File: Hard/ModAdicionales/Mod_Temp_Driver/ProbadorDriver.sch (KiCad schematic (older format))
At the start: 4 parts

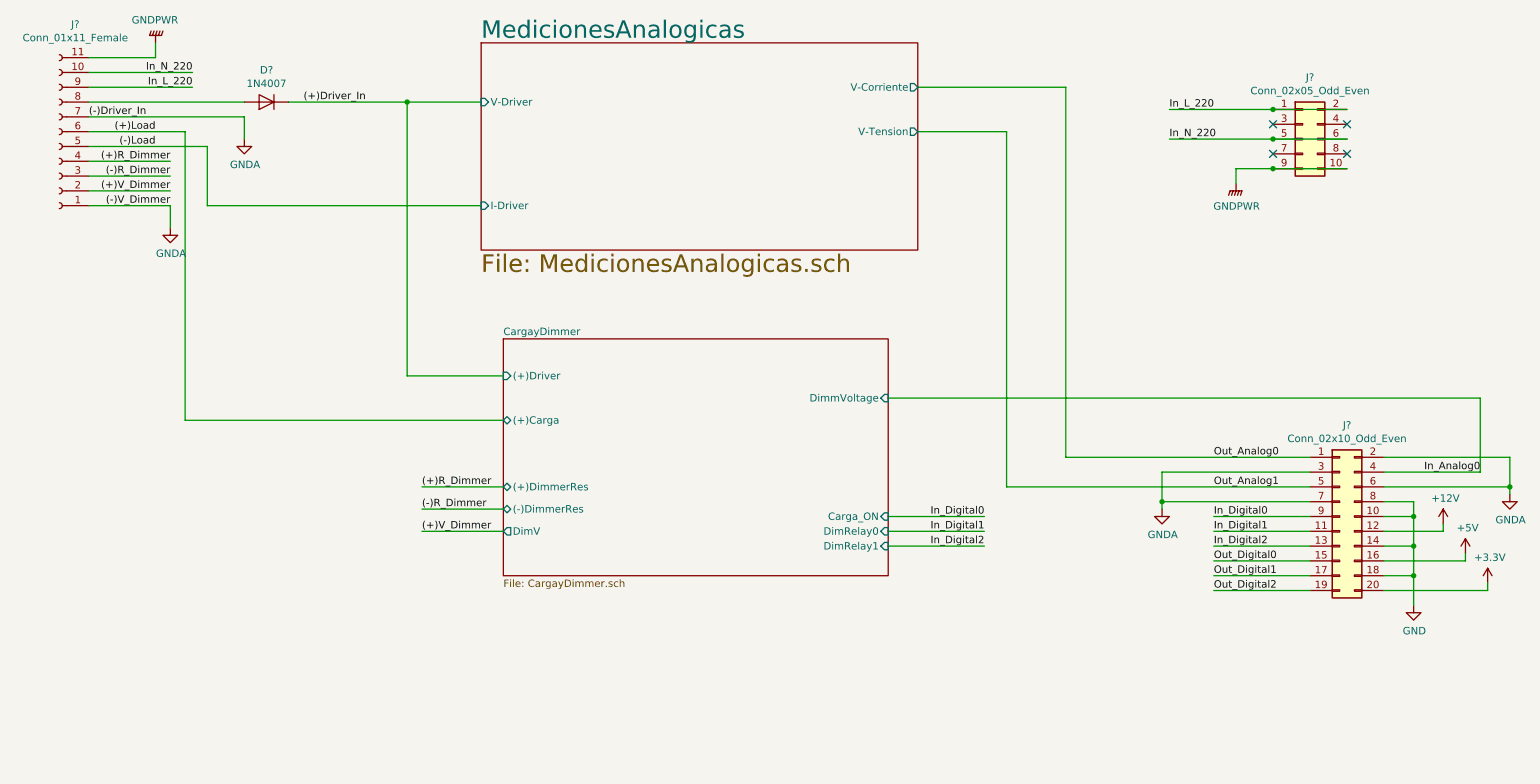
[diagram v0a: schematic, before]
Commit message: Primera correccion en modulos Adicionales y cambio de etapa de salida en modulo principal
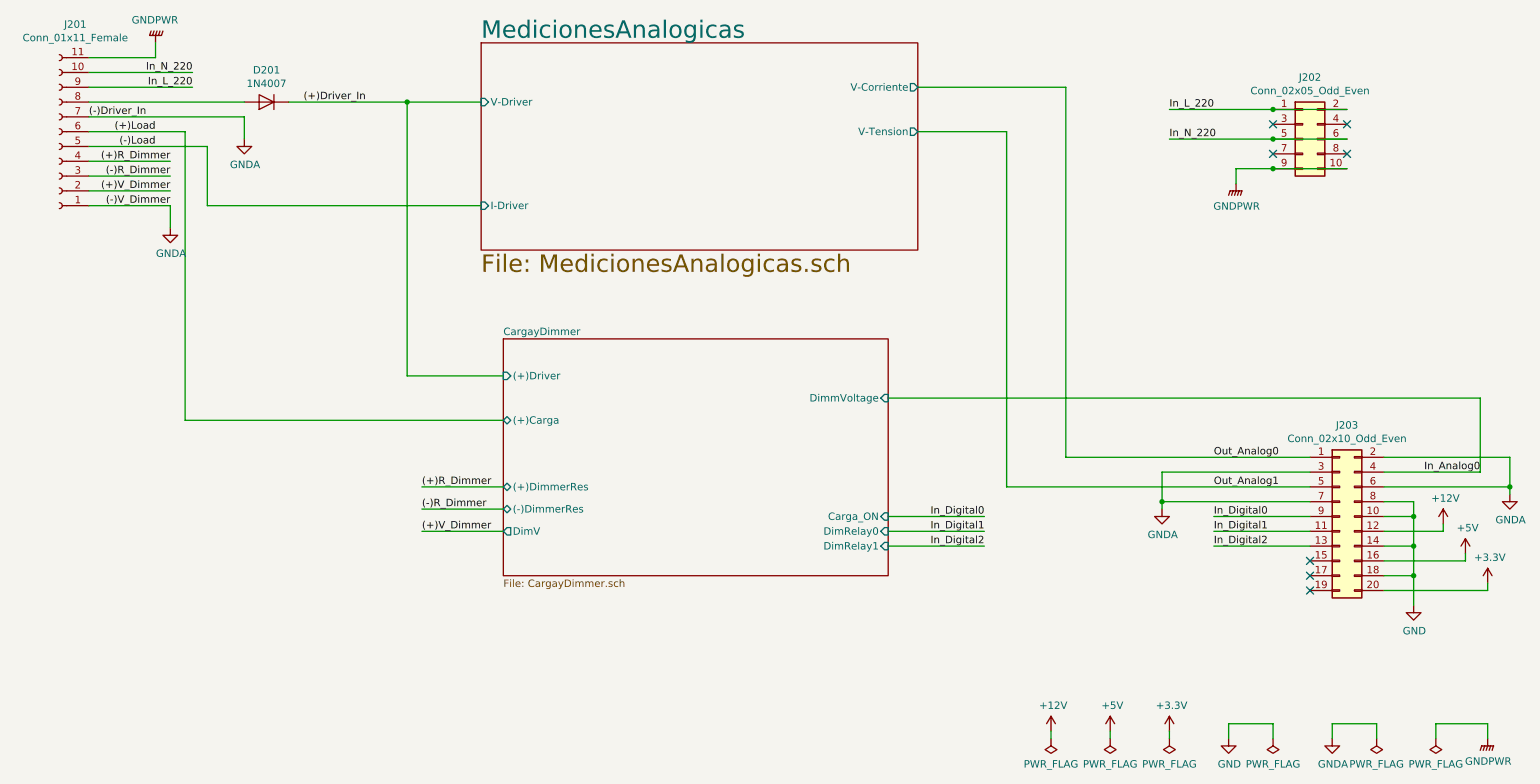
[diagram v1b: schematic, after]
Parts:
- gave numbers to parts that had none: 4
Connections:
- net Out_Digital0: no longer names the net of J203.15 (Pin_15)
- net Out_Digital1: no longer names the net of J203.17 (Pin_17)
- net Out_Digital2: no longer names the net of J203.19 (Pin_19)
- no-connect marks 4 -> 7
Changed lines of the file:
@@
 EESchema Schematic File Version 4
+LIBS:Mod_Temp_Driver-cache
 EELAYER 30 0
 EELAYER END
@@
 encoding utf-8
 Sheet 2 5
-Title ""
-Date ""
-Rev ""
-Comp ""
-Comment1 ""
+Title "Proyecto Final - Modulos Adicionales"
+Date "2020-06-02"
+Rev "1.0"
+Comp "CESE-FIUBA"
+Comment1 "Modulo Prueba de drivers"
 Comment2 ""
 Comment3 ""
@@
 $EndDescr
 $Comp
-L Connector_Generic:Conn_02x10_Odd_Even J?
+L Connector_Generic:Conn_02x10_Odd_Even J203
 U 1 1 5ED5A0E0
 P 9600 4650
-F 0 "J?" H 9650 5267 50  0000 C CNN
+F 0 "J203" H 9650 5267 50  0000 C CNN
 F 1 "Conn_02x10_Odd_Even" H 9650 5176 50  0000 C CNN
 F 2 "" H 9600 4650 50  0001 C CNN
@@
 Text Label 8750 4850 0    50   ~ 0
 In_Digital2
-Text Label 8750 4950 0    50   ~ 0
-Out_Digital0
-Text Label 8750 5050 0    50   ~ 0
-Out_Digital1
-Text Label 8750 5150 0    50   ~ 0
-Out_Digital2
 Text Label 10550 4350 2    50   ~ 0
 In_Analog0
 $Comp
-L power:+12V #PWR?
+L power:+12V #PWR0207
 U 1 1 5ED5A107
 P 10300 4700
-F 0 "#PWR?" H 10300 4550 50  0001 C CNN
+F 0 "#PWR0207" H 10300 4550 50  0001 C CNN
 F 1 "+12V" H 10315 4873 50  0000 C CNN
 F 2 "" H 10300 4700 50  0001 C CNN
@@
 $EndComp
 $Comp
-L power:+5V #PWR?
+L power:+5V #PWR0208
 U 1 1 5ED5A10D
 P 10450 4900
-F 0 "#PWR?" H 10450 4750 50  0001 C CNN
+F 0 "#PWR0208" H 10450 4750 50  0001 C CNN
 F 1 "+5V" H 10465 5073 50  0000 C CNN
 F 2 "" H 10450 4900 50  0001 C CNN
@@
 $EndComp
 $Comp
-L power:+3.3V #PWR?
+L power:+3.3V #PWR0209
 U 1 1 5ED5A113
 P 10600 5100
-F 0 "#PWR?" H 10600 4950 50  0001 C CNN
+F 0 "#PWR0209" H 10600 4950 50  0001 C CNN
 F 1 "+3.3V" H 10615 5273 50  0000 C CNN
 F 2 "" H 10600 5100 50  0001 C CNN
@@
 $EndComp
 $Comp
-L power:GND #PWR?
+L power:GND #PWR0206
 U 1 1 5ED5A119
 P 10100 5250
-F 0 "#PWR?" H 10100 5000 50  0001 C CNN
+F 0 "#PWR0206" H 10100 5000 50  0001 C CNN
 F 1 "GND" H 10105 5077 50  0000 C CNN
 F 2 "" H 10100 5250 50  0001 C CNN
@@
 $EndComp
 $Comp
-L power:GNDA #PWR?
+L power:GNDA #PWR0204
 U 1 1 5ED5A11F
 P 8400 4600
-F 0 "#PWR?" H 8400 4350 50  0001 C CNN
+F 0 "#PWR0204" H 8400 4350 50  0001 C CNN
 F 1 "GNDA" H 8405 4427 50  0000 C CNN
 F 2 "" H 8400 4600 50  0001 C CNN
@@
 	8400 4550 8400 4600
 $Comp
-L power:GNDA #PWR?
+L power:GNDA #PWR0210
 U 1 1 5ED5A12A
 P 10750 4500
-F 0 "#PWR?" H 10750 4250 50  0001 C CNN
+F 0 "#PWR0210" H 10750 4250 50  0001 C CNN
 F 1 "GNDA" H 10755 4327 50  0000 C CNN
 F 2 "" H 10750 4500 50  0001 C CNN
@@
 	10100 5050 10100 5250
 Wire Wire Line
-	9900 5150 10600 5150
-Wire Wire Line
 	10600 5150 10600 5100
 Wire Wire Line
-	9900 4950 10450 4950
-Wire Wire Line
 	10450 4950 10450 4900
 Wire Wire Line
-	9900 4750 10300 4750
-Wire Wire Line
 	10300 4750 10300 4700
 Wire Wire Line
@@
 Wire Wire Line
 	8750 4850 9400 4850
-Wire Wire Line
-	9400 4950 8750 4950
-Wire Wire Line
-	8750 5050 9400 5050
-Wire Wire Line
-	9400 5150 8750 5150
 Text Label 2600 1850 0    50   ~ 0
 (+)Driver_In
 $Comp
-L Connector:Conn_01x11_Female J?
+L Connector:Conn_01x11_Female J201
 U 1 1 5EDA75F8
 P 950 2050
-F 0 "J?" H 842 1325 50  0000 C CNN
+F 0 "J201" H 842 1325 50  0000 C CNN
 F 1 "Conn_01x11_Female" H 842 1416 50  0000 C CNN
 F 2 "" H 950 2050 50  0001 C CNN
@@
 	1600 1450 1600 1550
 $Comp
-L power:GNDPWR #PWR?
+L power:GNDPWR #PWR0201
 U 1 1 5EDAAA7D
 P 1600 1450
-F 0 "#PWR?" H 1600 1250 50  0001 C CNN
+F 0 "#PWR0201" H 1600 1250 50  0001 C CNN
 F 1 "GNDPWR" H 1604 1296 50  0000 C CNN
 F 2 "" H 1600 1400 50  0001 C CNN
@@
 	2200 1950 2200 2100
 $Comp
-L power:GNDA #PWR?
+L power:GNDA #PWR0203
 U 1 1 5EDB7AE8
 P 2200 2100
-F 0 "#PWR?" H 2200 1850 50  0001 C CNN
+F 0 "#PWR0203" H 2200 1850 50  0001 C CNN
 F 1 "GNDA" H 2205 1927 50  0000 C CNN
 F 2 "" H 2200 2100 50  0001 C CNN
@@
 (-)V_Dimmer
 $Comp
-L Diode:1N4007 D?
+L Diode:1N4007 D201
 U 1 1 5EFCD671
 P 2350 1850
-F 0 "D?" H 2350 1634 50  0000 C CNN
+F 0 "D201" H 2350 1634 50  0000 C CNN
 F 1 "1N4007" H 2350 1725 50  0000 C CNN
 F 2 "Diode_THT:D_DO-41_SOD81_P10.16mm_Horizontal" H 2350 1675 50  0001 C CNN
@@
 $EndSheet
 $Comp
-L Connector_Generic:Conn_02x05_Odd_Even J?
+L Connector_Generic:Conn_02x05_Odd_Even J202
 U 1 1 5F1BC542
 P 9350 2100
-AR Path="/5ED5374F/5F1BC542" Ref="J?"  Part="1"
+AR Path="/5ED5374F/5F1BC542" Ref="J202"  Part="1"
 AR Path="/5ED5374F/5F0ECABF/5F1BC542" Ref="J?"  Part="1"
-F 0 "J?" H 9400 2517 50  0000 C CNN
+F 0 "J202" H 9400 2517 50  0000 C CNN
 F 1 "Conn_02x05_Odd_Even" H 9400 2426 50  0000 C CNN
 F 2 "" H 9350 2100 50  0001 C CNN
@@
 In_L_220
 $Comp
-L power:GNDPWR #PWR?
+L power:GNDPWR #PWR0205
 U 1 1 5F1BC54A
 P 8900 2400
-AR Path="/5ED5374F/5F1BC54A" Ref="#PWR?"  Part="1"
+AR Path="/5ED5374F/5F1BC54A" Ref="#PWR0205"  Part="1"
 AR Path="/5ED5374F/5F0ECABF/5F1BC54A" Ref="#PWR?"  Part="1"
-F 0 "#PWR?" H 8900 2200 50  0001 C CNN
+F 0 "#PWR0205" H 8900 2200 50  0001 C CNN
 F 1 "GNDPWR" H 8904 2246 50  0000 C CNN
 F 2 "" H 8900 2350 50  0001 C CNN
@@
 	1700 2550 1700 2700
 $Comp
-L power:GNDA #PWR?
+L power:GNDA #PWR0202
 U 1 1 5F3DBE4C
 P 1700 2700
-F 0 "#PWR?" H 1700 2450 50  0001 C CNN
+F 0 "#PWR0202" H 1700 2450 50  0001 C CNN
 F 1 "GNDA" H 1705 2527 50  0000 C CNN
 F 2 "" H 1700 2700 50  0001 C CNN
@@
 	1    0    0    -1
 $EndComp
+NoConn ~ 9400 4950
+NoConn ~ 9400 5050
+NoConn ~ 9400 5150
+$Comp
+L power:+12V #PWR0101
+U 1 1 5EE6D5BC
+P 7650 6100
+F 0 "#PWR0101" H 7650 5950 50  0001 C CNN
+F 1 "+12V" H 7665 6273 50  0000 C CNN
+F 2 "" H 7650 6100 50  0001 C CNN
+F 3 "" H 7650 6100 50  0001 C CNN
+	1    7650 6100
+	1    0    0    -1
+$EndComp
+$Comp
+L power:+5V #PWR0102
+U 1 1 5EE6D5C2
+P 8050 6100
+F 0 "#PWR0102" H 8050 5950 50  0001 C CNN
+F 1 "+5V" H 8065 6273 50  0000 C CNN
+F 2 "" H 8050 6100 50  0001 C CNN
+F 3 "" H 8050 6100 50  0001 C CNN
+	1    8050 6100
+	1    0    0    -1
+$EndComp
+$Comp
+L power:+3.3V #PWR0103
+U 1 1 5EE6D5C8
+P 8450 6100
+F 0 "#PWR0103" H 8450 5950 50  0001 C CNN
+F 1 "+3.3V" H 8465 6273 50  0000 C CNN
+F 2 "" H 8450 6100 50  0001 C CNN
+F 3 "" H 8450 6100 50  0001 C CNN
+	1    8450 6100
+	1    0    0    -1
+$EndComp
+Wire Wire Line
+	8450 6150 8450 6100
+Wire Wire Line
+	8050 6150 8050 6100
+Wire Wire Line
+	7650 6150 7650 6100
+$Comp
+L power:PWR_FLAG #FLG0101
+U 1 1 5EE6D5D4
+P 8050 6150
+F 0 "#FLG0101" H 8050 6225 50  0001 C CNN
+F 1 "PWR_FLAG" H 8050 6323 50  0000 C CNN
+F 2 "" H 8050 6150 50  0001 C CNN
+F 3 "~" H 8050 6150 50  0001 C CNN
+	1    8050 6150
+	-1   0    0    1
+$EndComp
+$Comp
+L power:PWR_FLAG #FLG0102
+U 1 1 5EE6D5DC
+P 7650 6150
+F 0 "#FLG0102" H 7650 6225 50  0001 C CNN
+F 1 "PWR_FLAG" H 7650 6323 50  0000 C CNN
+F 2 "" H 7650 6150 50  0001 C CNN
+F 3 "~" H 7650 6150 50  0001 C CNN
+	1    7650 6150
+	-1   0    0    1
+$EndComp
+$Comp
+L power:PWR_FLAG #FLG0103
+U 1 1 5EE823D4
+P 8450 6150
+F 0 "#FLG0103" H 8450 6225 50  0001 C CNN
+F 1 "PWR_FLAG" H 8450 6323 50  0000 C CNN
+F 2 "" H 8450 6150 50  0001 C CNN
+F 3 "~" H 8450 6150 50  0001 C CNN
+	1    8450 6150
+	-1   0    0    1
+$EndComp
+$Comp
+L power:GND #PWR0104
+U 1 1 5EE8980A
+P 8850 6150
+F 0 "#PWR0104" H 8850 5900 50  0001 C CNN
+F 1 "GND" H 8855 5977 50  0000 C CNN
+F 2 "" H 8850 6150 50  0001 C CNN
+F 3 "" H 8850 6150 50  0001 C CNN
+	1    8850 6150
+	1    0    0    -1
+$EndComp
+$Comp
+L power:PWR_FLAG #FLG0106
+U 1 1 5EE8BBA8
+P 9150 6150
+F 0 "#FLG0106" H 9150 6225 50  0001 C CNN
+F 1 "PWR_FLAG" H 9150 6323 50  0000 C CNN
+F 2 "" H 9150 6150 50  0001 C CNN
+F 3 "~" H 9150 6150 50  0001 C CNN
+	1    9150 6150
+	-1   0    0    1
+$EndComp
+Wire Wire Line
+	9150 6150 9150 6050
+Wire Wire Line
+	9150 6050 8850 6050
+Wire Wire Line
+	8850 6050 8850 6150
+Wire Wire Line
+	9900 5150 10600 5150
+Wire Wire Line
+	9900 4950 10450 4950
+Wire Wire Line
+	9900 4750 10300 4750
+$Comp
+L power:PWR_FLAG #FLG0107
+U 1 1 5EE96E0D
+P 9850 6150
+F 0 "#FLG0107" H 9850 6225 50  0001 C CNN
+F 1 "PWR_FLAG" H 9850 6323 50  0000 C CNN
+F 2 "" H 9850 6150 50  0001 C CNN
+F 3 "~" H 9850 6150 50  0001 C CNN
+	1    9850 6150
+	-1   0    0    1
+$EndComp
+Wire Wire Line
+	9850 6150 9850 6050
+Wire Wire Line
+	9850 6050 9550 6050
+Wire Wire Line
+	9550 6050 9550 6150
+$Comp
+L power:GNDA #PWR0105
+U 1 1 5EE9BBA8
+P 9550 6150
+F 0 "#PWR0105" H 9550 5900 50  0001 C CNN
+F 1 "GNDA" H 9555 5977 50  0000 C CNN
+F 2 "" H 9550 6150 50  0001 C CNN
+F 3 "" H 9550 6150 50  0001 C CNN
+	1    9550 6150
+	1    0    0    -1
+$EndComp
+$Comp
+L power:GNDPWR #PWR0107
+U 1 1 5EEDA7EC
+P 10600 6150
+F 0 "#PWR0107" H 10600 5950 50  0001 C CNN
+F 1 "GNDPWR" H 10604 5996 50  0000 C CNN
+F 2 "" H 10600 6100 50  0001 C CNN
+F 3 "" H 10600 6100 50  0001 C CNN
+	1    10600 6150
+	1    0    0    -1
+$EndComp
+$Comp
+L power:PWR_FLAG #FLG0105
+U 1 1 5EEDA7F2
+P 10250 6150
+F 0 "#FLG0105" H 10250 6225 50  0001 C CNN
+F 1 "PWR_FLAG" H 10250 6323 50  0000 C CNN
+F 2 "" H 10250 6150 50  0001 C CNN
+F 3 "~" H 10250 6150 50  0001 C CNN
+	1    10250 6150
+	-1   0    0    1
+$EndComp
+Wire Wire Line
+	10250 6050 10600 6050
+Wire Wire Line
+	10600 6050 10600 6150
+Wire Wire Line
+	10250 6050 10250 6150
 $EndSCHEMATC

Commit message: Asignacion de footprints Modulos adicionales
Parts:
- J201: footprint (none) -> TerminalBlock_Altech:Altech_AK300_1x11_P5.00mm_45-Degree
- J202: footprint (none) -> Connector_PinHeader_2.54mm:PinHeader_2x05_P2.54mm_Horizontal
- J203: footprint (none) -> Connector_PinHeader_2.54mm:PinHeader_2x10_P2.54mm_Horizontal
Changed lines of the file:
@@
 F 0 "J203" H 9650 5267 50  0000 C CNN
 F 1 "Conn_02x10_Odd_Even" H 9650 5176 50  0000 C CNN
-F 2 "" H 9600 4650 50  0001 C CNN
+F 2 "Connector_PinHeader_2.54mm:PinHeader_2x10_P2.54mm_Horizontal" H 9600 4650 50  0001 C CNN
 F 3 "~" H 9600 4650 50  0001 C CNN
 	1    9600 4650
@@
 F 0 "J201" H 842 1325 50  0000 C CNN
 F 1 "Conn_01x11_Female" H 842 1416 50  0000 C CNN
-F 2 "" H 950 2050 50  0001 C CNN
+F 2 "TerminalBlock_Altech:Altech_AK300_1x11_P5.00mm_45-Degree" H 950 2050 50  0001 C CNN
 F 3 "~" H 950 2050 50  0001 C CNN
 	1    950  2050
@@
 F 0 "J202" H 9400 2517 50  0000 C CNN
 F 1 "Conn_02x05_Odd_Even" H 9400 2426 50  0000 C CNN
-F 2 "" H 9350 2100 50  0001 C CNN
+F 2 "Connector_PinHeader_2.54mm:PinHeader_2x05_P2.54mm_Horizontal" H 9350 2100 50  0001 C CNN
 F 3 "~" H 9350 2100 50  0001 C CNN
 	1    9350 2100

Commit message: Inicio placement de componentes en Modulos Adicionales
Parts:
- added H201, H202, H203, H204: MountingHole, MountingHole:MountingHole_3.2mm_M3, symbol Mechanical:MountingHole
- J201: footprint TerminalBlock_Altech:Altech_AK300_1x11_P5.00mm_45-Degree -> Conectores:TerminalBlock_bornier-11_P5.00mm
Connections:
- net (+)R_Dimmer: now also J201.8 (Pin_8); no longer J201.4 (Pin_4)
- net (+)V_Dimmer: now also J201.10 (Pin_10); no longer J201.2 (Pin_2)
- net (-)Load: now also J201.7 (Pin_7); no longer J201.5 (Pin_5)
- net (-)R_Dimmer: now also J201.9 (Pin_9); no longer J201.3 (Pin_3)
- net GNDA: now also J201.11 (Pin_11), J201.5 (Pin_5); no longer J201.1 (Pin_1), J201.7 (Pin_7)
- net GNDPWR: now also J201.1 (Pin_1); no longer J201.11 (Pin_11)
- net In_L_220: now also J201.3 (Pin_3); no longer J201.9 (Pin_9)
- net In_N_220: now also J201.2 (Pin_2); no longer J201.10 (Pin_10)
- net at D201.2 (A): now also J201.4 (Pin_4); no longer J201.8 (Pin_8)
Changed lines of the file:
@@
 EESchema Schematic File Version 4
-LIBS:Mod_Temp_Driver-cache
 EELAYER 30 0
 EELAYER END
@@
 Comment4 ""
 $EndDescr
-$Comp
-L Connector_Generic:Conn_02x10_Odd_Even J203
-U 1 1 5ED5A0E0
-P 9600 4650
-F 0 "J203" H 9650 5267 50  0000 C CNN
-F 1 "Conn_02x10_Odd_Even" H 9650 5176 50  0000 C CNN
-F 2 "Connector_PinHeader_2.54mm:PinHeader_2x10_P2.54mm_Horizontal" H 9600 4650 50  0001 C CNN
-F 3 "~" H 9600 4650 50  0001 C CNN
-	1    9600 4650
-	1    0    0    -1
-$EndComp
 Text Label 8750 4250 0    50   ~ 0
 Out_Analog0
@@
 Text Label 2600 1850 0    50   ~ 0
 (+)Driver_In
-$Comp
-L Connector:Conn_01x11_Female J201
-U 1 1 5EDA75F8
-P 950 2050
-F 0 "J201" H 842 1325 50  0000 C CNN
-F 1 "Conn_01x11_Female" H 842 1416 50  0000 C CNN
-F 2 "TerminalBlock_Altech:Altech_AK300_1x11_P5.00mm_45-Degree" H 950 2050 50  0001 C CNN
-F 3 "~" H 950 2050 50  0001 C CNN
-	1    950  2050
-	-1   0    0    1
-$EndComp
 Text Label 1850 1650 2    50   ~ 0
 In_N_220
@@
 	1    0    0    -1
 $EndComp
-Text Label 1600 2050 2    50   ~ 0
-(+)Load
-Text Label 1600 2150 2    50   ~ 0
-(-)Load
 Text Label 1700 2250 2    50   ~ 0
 (+)R_Dimmer
@@
 Text Label 1700 2550 2    50   ~ 0
 (-)V_Dimmer
-$Comp
-L Diode:1N4007 D201
-U 1 1 5EFCD671
-P 2350 1850
-F 0 "D201" H 2350 1634 50  0000 C CNN
-F 1 "1N4007" H 2350 1725 50  0000 C CNN
-F 2 "Diode_THT:D_DO-41_SOD81_P10.16mm_Horizontal" H 2350 1675 50  0001 C CNN
-F 3 "http://www.vishay.com/docs/88503/1n4001.pdf" H 2350 1850 50  0001 C CNN
-	1    2350 1850
-	-1   0    0    1
-$EndComp
 Wire Wire Line
 	1150 1850 2200 1850
@@
 F5 "V-Driver" I L 3800 1850 50
 $EndSheet
-$Comp
-L Connector_Generic:Conn_02x05_Odd_Even J202
-U 1 1 5F1BC542
-P 9350 2100
-AR Path="/5ED5374F/5F1BC542" Ref="J202"  Part="1"
-AR Path="/5ED5374F/5F0ECABF/5F1BC542" Ref="J?"  Part="1"
-F 0 "J202" H 9400 2517 50  0000 C CNN
-F 1 "Conn_02x05_Odd_Even" H 9400 2426 50  0000 C CNN
-F 2 "Connector_PinHeader_2.54mm:PinHeader_2x05_P2.54mm_Horizontal" H 9350 2100 50  0001 C CNN
-F 3 "~" H 9350 2100 50  0001 C CNN
-	1    9350 2100
-	1    0    0    -1
-$EndComp
 Text Label 8450 2100 0    50   ~ 0
 In_N_220
@@
 	3300 1850 3800 1850
 Wire Wire Line
-	1800 2050 1150 2050
-Wire Wire Line
 	1800 4000 3950 4000
 Text Label 3400 4450 0    50   ~ 0
@@
 	1150 1950 2200 1950
 Wire Wire Line
-	1800 2050 1800 4000
-Wire Wire Line
-	1950 2150 1950 2550
-Wire Wire Line
 	1950 2550 3800 2550
-Wire Wire Line
-	1150 2150 1950 2150
 Wire Wire Line
 	1150 2550 1700 2550
@@
 Wire Wire Line
 	10250 6050 10250 6150
+Wire Wire Line
+	1950 2150 1950 2550
+Wire Wire Line
+	1800 2050 1800 4000
+Wire Wire Line
+	1800 2050 1150 2050
+Text Label 1600 2050 2    50   ~ 0
+(+)Load
+Wire Wire Line
+	1150 2150 1950 2150
+Text Label 1600 2150 2    50   ~ 0
+(-)Load
+$Comp
+L Connector_Generic:Conn_02x10_Odd_Even J203
+U 1 1 5ED5A0E0
+P 9600 4650
+F 0 "J203" H 9650 5267 50  0000 C CNN
+F 1 "Conn_02x10_Odd_Even" H 9650 5176 50  0000 C CNN
+F 2 "Connector_PinHeader_2.54mm:PinHeader_2x10_P2.54mm_Horizontal" H 9600 4650 50  0001 C CNN
+F 3 "~" H 9600 4650 50  0001 C CNN
+	1    9600 4650
+	1    0    0    -1
+$EndComp
+$Comp
+L Connector:Conn_01x11_Female J201
+U 1 1 5EDA75F8
+P 950 2050
+F 0 "J201" H 842 1325 50  0000 C CNN
+F 1 "Conn_01x11_Female" H 842 1416 50  0000 C CNN
+F 2 "Conectores:TerminalBlock_bornier-11_P5.00mm" H 950 2050 50  0001 C CNN
+F 3 "~" H 950 2050 50  0001 C CNN
+	1    950  2050
+	-1   0    0    -1
+$EndComp
+$Comp
+L Diode:1N4007 D201
+U 1 1 5EFCD671
+P 2350 1850
+F 0 "D201" H 2350 1634 50  0000 C CNN
+F 1 "1N4007" H 2350 1725 50  0000 C CNN
+F 2 "Diode_THT:D_DO-41_SOD81_P10.16mm_Horizontal" H 2350 1675 50  0001 C CNN
+F 3 "http://www.vishay.com/docs/88503/1n4001.pdf" H 2350 1850 50  0001 C CNN
+	1    2350 1850
+	-1   0    0    1
+$EndComp
+$Comp
+L Connector_Generic:Conn_02x05_Odd_Even J202
+U 1 1 5F1BC542
+P 9350 2100
+AR Path="/5ED5374F/5F1BC542" Ref="J202"  Part="1"
+AR Path="/5ED5374F/5F0ECABF/5F1BC542" Ref="J?"  Part="1"
+F 0 "J202" H 9400 2517 50  0000 C CNN
+F 1 "Conn_02x05_Odd_Even" H 9400 2426 50  0000 C CNN
+F 2 "Connector_PinHeader_2.54mm:PinHeader_2x05_P2.54mm_Horizontal" H 9350 2100 50  0001 C CNN
+F 3 "~" H 9350 2100 50  0001 C CNN
+	1    9350 2100
+	1    0    0    -1
+$EndComp
+$Comp
+L Mechanical:MountingHole H201
+U 1 1 5ED7D0A9
+P 1600 5700
+F 0 "H201" H 1700 5746 50  0000 L CNN
+F 1 "MountingHole" H 1700 5655 50  0000 L CNN
+F 2 "MountingHole:MountingHole_3.2mm_M3" H 1600 5700 50  0001 C CNN
+F 3 "~" H 1600 5700 50  0001 C CNN
+	1    1600 5700
+	1    0    0    -1
+$EndComp
+$Comp
+L Mechanical:MountingHole H203
+U 1 1 5ED7D6D3
+P 2600 5700
+F 0 "H203" H 2700 5746 50  0000 L CNN
+F 1 "MountingHole" H 2700 5655 50  0000 L CNN
+F 2 "MountingHole:MountingHole_3.2mm_M3" H 2600 5700 50  0001 C CNN
+F 3 "~" H 2600 5700 50  0001 C CNN
+	1    2600 5700
+	1    0    0    -1
+$EndComp
+$Comp
+L Mechanical:MountingHole H202
+U 1 1 5ED7F908
+P 1600 6100
+F 0 "H202" H 1700 6146 50  0000 L CNN
+F 1 "MountingHole" H 1700 6055 50  0000 L CNN
+F 2 "MountingHole:MountingHole_3.2mm_M3" H 1600 6100 50  0001 C CNN
+F 3 "~" H 1600 6100 50  0001 C CNN
+	1    1600 6100
+	1    0    0    -1
+$EndComp
+$Comp
+L Mechanical:MountingHole H204
+U 1 1 5ED81CED
+P 2600 6100
+F 0 "H204" H 2700 6146 50  0000 L CNN
+F 1 "MountingHole" H 2700 6055 50  0000 L CNN
+F 2 "MountingHole:MountingHole_3.2mm_M3" H 2600 6100 50  0001 C CNN
+F 3 "~" H 2600 6100 50  0001 C CNN
+	1    2600 6100
+	1    0    0    -1
+$EndComp
 $EndSCHEMATC
